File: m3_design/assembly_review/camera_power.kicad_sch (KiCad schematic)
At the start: 22 parts, among them U7 TPS259570DSGR, U8 AP63200WU-7

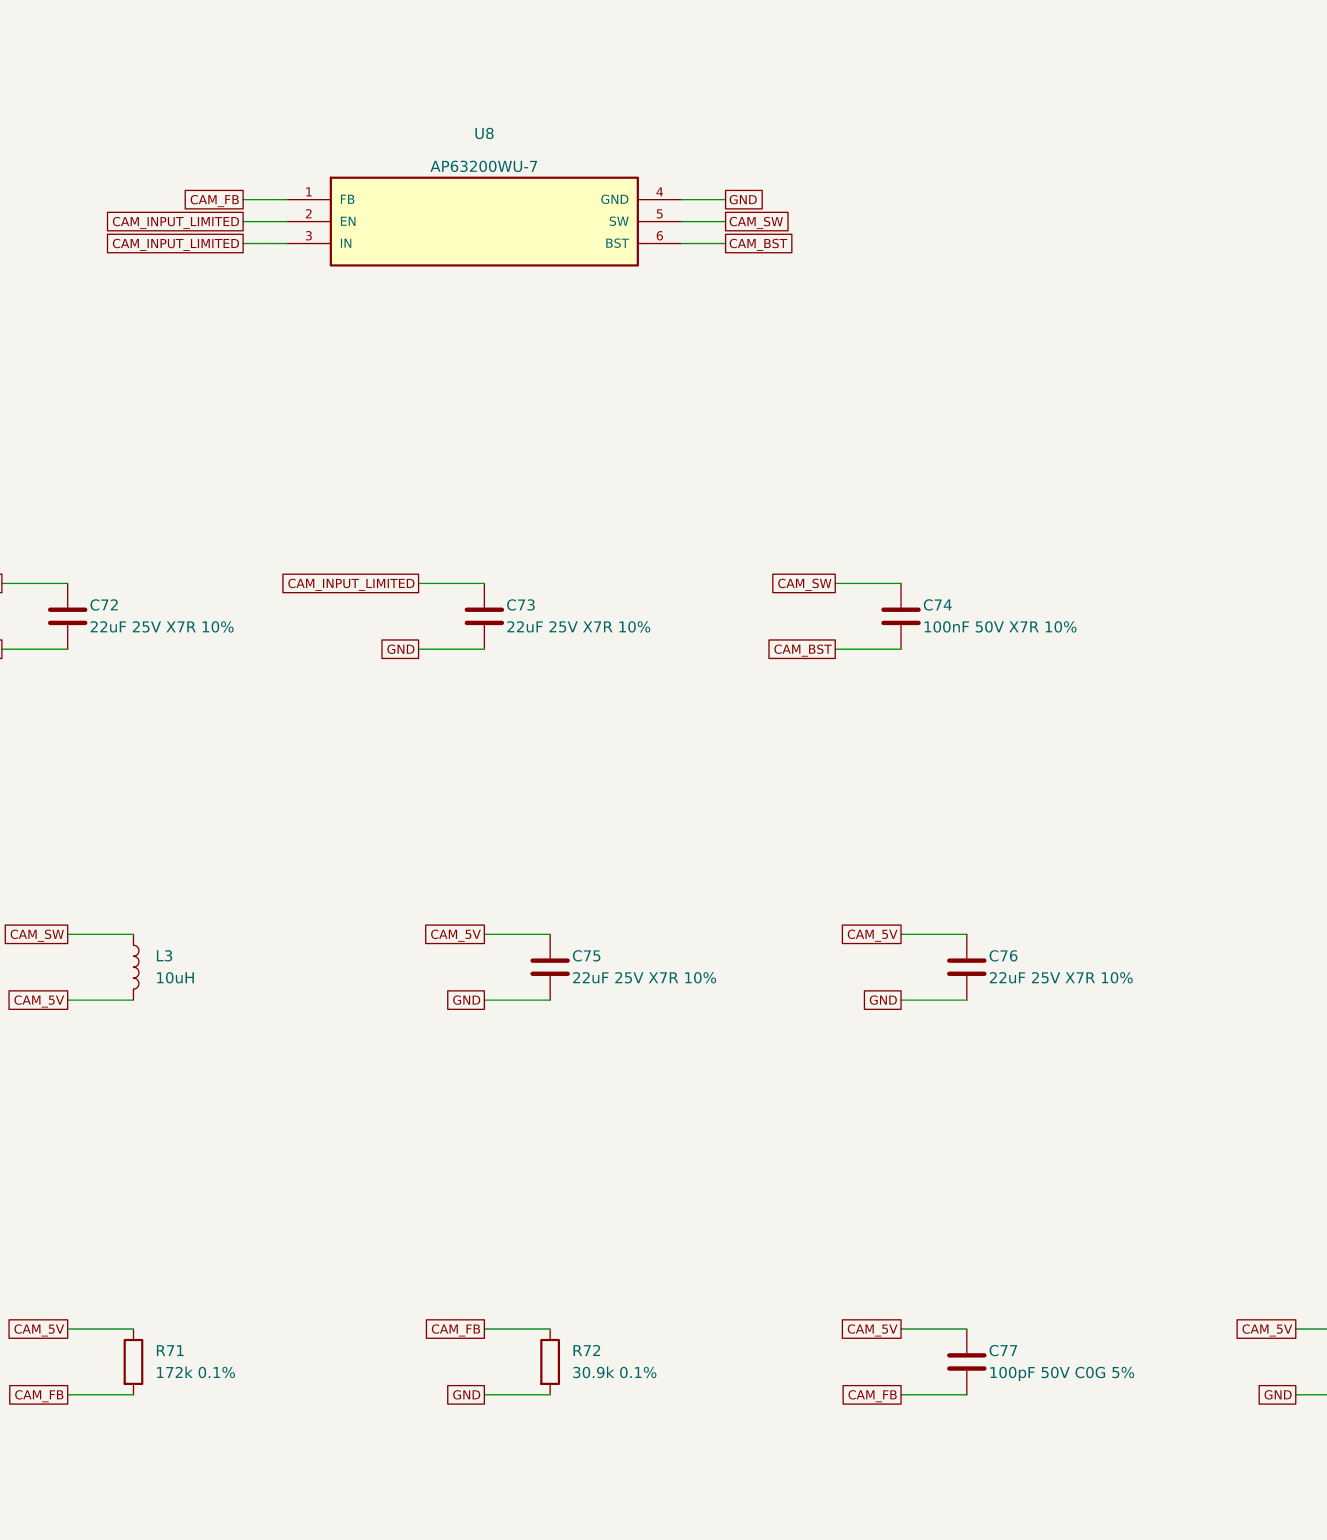
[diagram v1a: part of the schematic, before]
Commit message: Make R2 orderable: stocked drop-ins, JLC placement corrections, ordering guide
- Stock (JLC assembly API): U8 AP63200 -> AP63300WU-7 (same TSOT26 pinout,
  VFB, fsw), L3 -> SRP5030T-6R8M (same body/land, AP63300 Table 1), C77
  100p -> 47p (Table 1), C84 25SVPF330M -> 35SVPK330M (same OS-CON F12).
  Every BOM line now has JLC stock for 5 boards except U6 SAM-M10Q
  (consign / Global Sourcing; DigiKey has stock).
- tools/jlc_orient.py matches each footprint pad-by-pad to the LCSC/EasyEDA
  footprint of its LCSC code; export_fab.py applies the rotation/offset.
  Without it U7, U8, U10, U11, U12, U13, D121 and LED2 would be rotated.
- tools/jlc_stock.py: repeatable stock check; fab/stock_check.json.
- JLC_Assembly field: U6 consign note, J2/J123 hand-cut from one 1x40 strip.
- docs/ORDERING.md: PCB options, PCBA, preview checklist, off-board parts.

DRC 0 / unconnected 0 / parity 0 / ERC 0, audit OK; contract OK;
tests 173/112/12 pass; sim 135 PASS.

Co-Authored-By: Claude Opus 5.5 (1M context) <noreply@anthropic.com>
Claude-Session: https://claude.ai/code/session_01DdkfTxR7SVyv9xZNmPk9vB
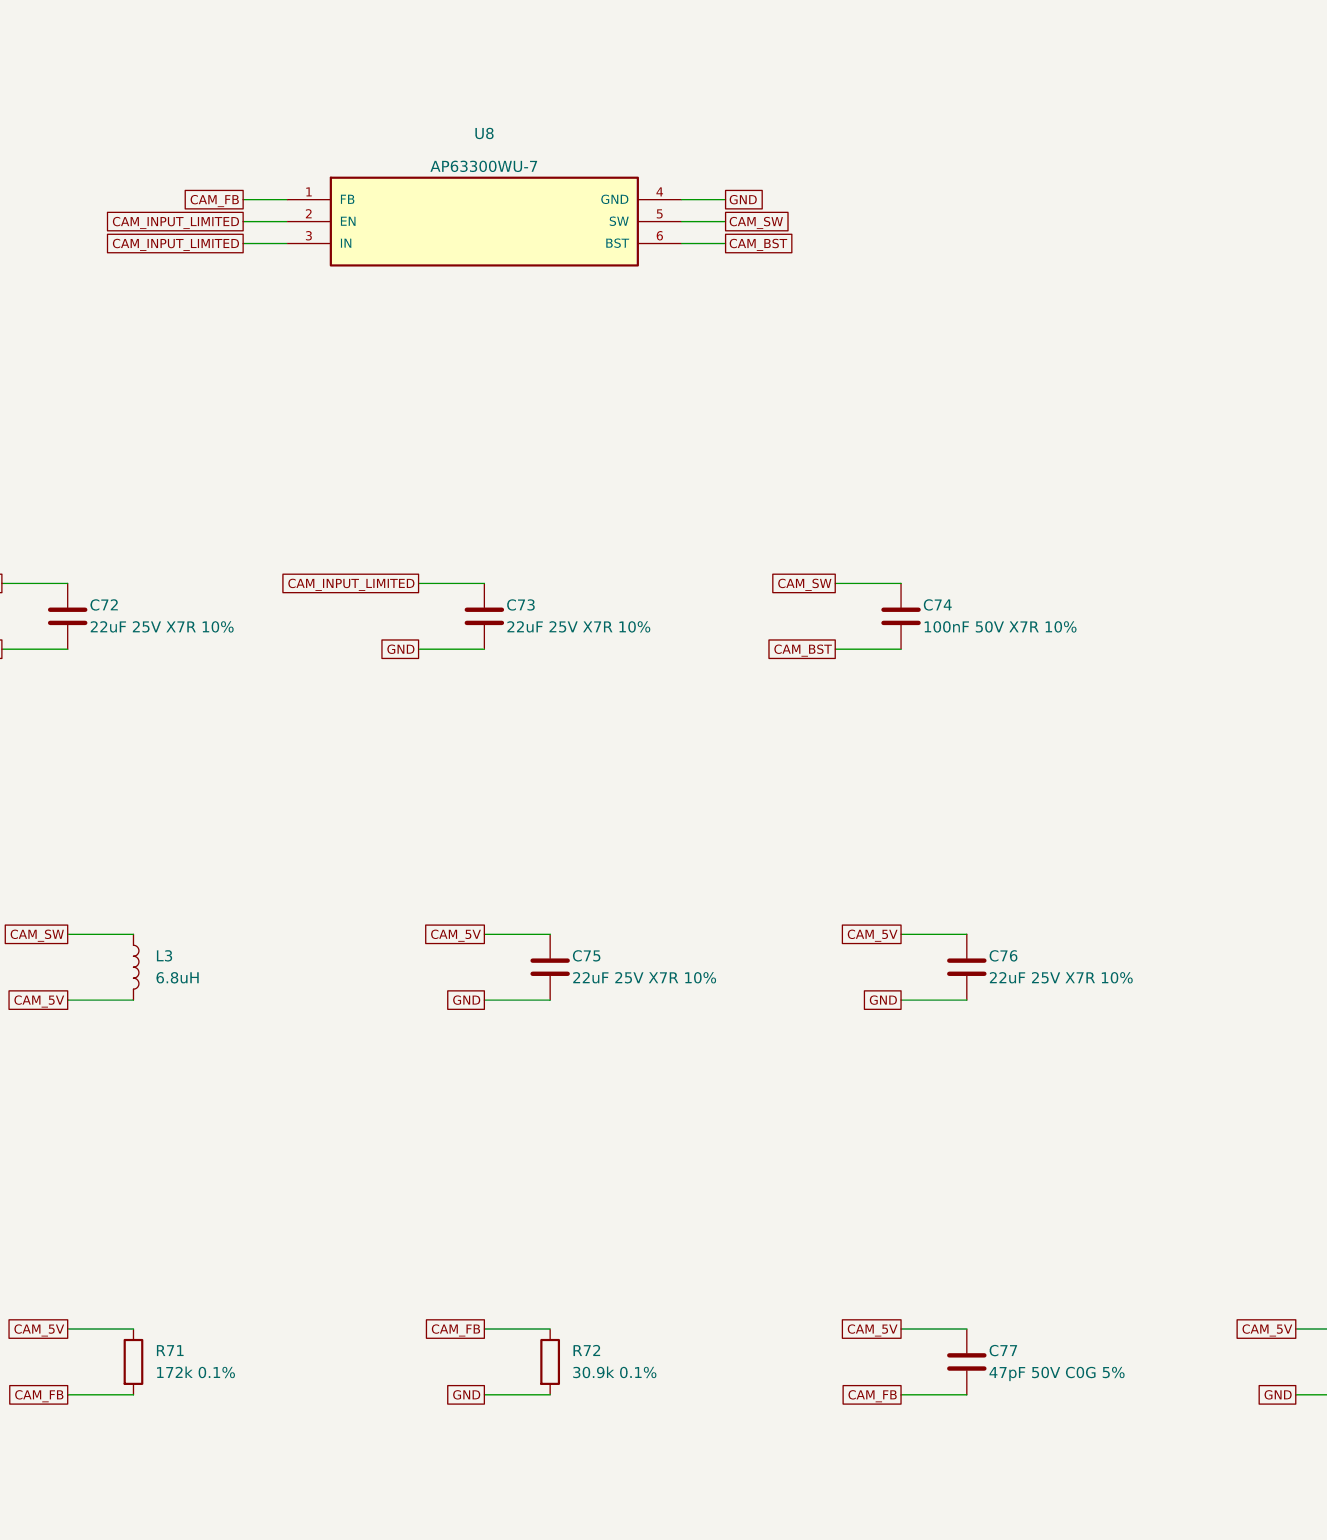
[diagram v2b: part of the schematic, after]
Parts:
- C77: value 100pF 50V C0G 5% -> 47pF 50V C0G 5%; LCSC C14858 -> C1671; LCSC Part C14858 -> C1671; Manufacturer Part CL10C101JB8NNNC -> CL10C470JB8NNNC
- L3: value 10uH -> 6.8uH; LCSC C3223923 -> C1329837; LCSC Part C3223923 -> C1329837; Manufacturer Part SRP5030TA-100M -> SRP5030T-6R8M
- U8: value AP63200WU-7 -> AP63300WU-7; LCSC C2071868 -> C2158012
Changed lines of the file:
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@@
 				(font
 					(size 1.27 1.27))))
-		(property "Value" "AP63200WU-7"
+		(property "Value" "AP63300WU-7"
 			(at 276.86 69.85 0)
 			(effects
@@
 				(font
 					(size 1.27 1.27))))
-		(property "LCSC" "C2071868"
+		(property "LCSC" "C2158012"
 			(at 276.86 76.2 0)
 			(hide yes)
@@
 					(size 1.27 1.27))
 				(justify left)))
-		(property "Value" "10uH"
+		(property "Value" "6.8uH"
 			(at 238.76 163.82999999999998 0)
 			(effects
@@
 					(size 1.27 1.27))
 				(justify left)))
-		(property "LCSC" "C3223923"
+		(property "LCSC" "C1329837"
 			(at 236.22 162.56 0)
 			(hide yes)
@@
 				(font
 					(size 1.27 1.27))))
-		(property "Manufacturer Part" "SRP5030TA-100M"
+		(property "Manufacturer Part" "SRP5030T-6R8M"
 			(at 236.22 162.56 0)
 			(hide yes)
@@
 				(font
 					(size 1.27 1.27))))
-		(property "LCSC Part" "C3223923"
+		(property "LCSC Part" "C1329837"
 			(at 236.22 162.56 0)
 			(hide yes)
@@
 					(size 1.27 1.27))
 				(justify left)))
-		(property "Value" "100pF 50V C0G 5%"
+		(property "Value" "47pF 50V C0G 5%"
 			(at 335.28000000000003 209.54999999999998 0)
 			(effects
@@
 					(size 1.27 1.27))
 				(justify left)))
-		(property "LCSC" "C14858"
+		(property "LCSC" "C1671"
 			(at 332.74 208.28 0)
 			(hide yes)
@@
 				(font
 					(size 1.27 1.27))))
-		(property "Manufacturer Part" "CL10C101JB8NNNC"
+		(property "Manufacturer Part" "CL10C470JB8NNNC"
 			(at 332.74 208.28 0)
 			(hide yes)
@@
 				(font
 					(size 1.27 1.27))))
-		(property "LCSC Part" "C14858"
+		(property "LCSC Part" "C1671"
 			(at 332.74 208.28 0)
 			(hide yes)

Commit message: M3-ASSY-R3: 1k 1% resistors to JLC Basic, regenerate fab package, cost gate
R74/R77/R100/R101/R103: C22548 (Yageo RC0603FR-071KL) -> C21190 (UNI-ROYAL
0603WAF1001T5E), same 1k 1% 100 ppm 0.1 W 75 V 0603 land. The 100 nF C1591 ->
C14663 swap was not made: C128/C140 sit on the pyro outputs and no DC-bias data
exists for the replacement, so the line stays extended either way.
jlc_orient: C21190 via a same-footprint donor (EasyEDA API returned 403).
export_fab: 75 lines, 180 placed, no missing LCSC, no unverified rotation.
jlc_stock --boards 5: short only U4 ICM-45686 (JLC stock 0, protected).
jlc_cost: parts $54.94/board at 5 boards, 48 unique extended codes (gate counts
codes, not rows). check.sh all zero.

Co-Authored-By: Claude Opus 5.5 <noreply@anthropic.com>
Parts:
- R74, R77: LCSC C22548 -> C21190; LCSC Part C22548 -> C21190; Manufacturer Yageo -> UNI-ROYAL(Uniroyal Elec); Manufacturer Part RC0603FR-071KL -> 0603WAF1001T5E
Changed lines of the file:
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@@
 					(size 1.27 1.27))
 				(justify left)))
-		(property "LCSC" "C22548"
+		(property "LCSC" "C21190"
 			(at 53.34 213.36 0)
 			(hide yes)
@@
 					(reference "R74")
 					(unit 1))))
-		(property "Manufacturer" "Yageo"
+		(property "Manufacturer" "UNI-ROYAL(Uniroyal Elec)"
 			(at 53.34 213.36 0)
 			(hide yes)
@@
 				(font
 					(size 1.27 1.27))))
-		(property "Manufacturer Part" "RC0603FR-071KL"
+		(property "Manufacturer Part" "0603WAF1001T5E"
 			(at 53.34 213.36 0)
 			(hide yes)
@@
 				(font
 					(size 1.27 1.27))))
-		(property "LCSC Part" "C22548"
+		(property "LCSC Part" "C21190"
 			(at 53.34 213.36 0)
 			(hide yes)
@@
 					(size 1.27 1.27))
 				(justify left)))
-		(property "LCSC" "C22548"
+		(property "LCSC" "C21190"
 			(at 104.14 254 0)
 			(hide yes)
@@
 					(reference "R77")
 					(unit 1))))
-		(property "Manufacturer" "Yageo"
-			(at 104.14 254 0)
-			(hide yes)
-			(effects
-				(font
-					(size 1.27 1.27))))
-		(property "Manufacturer Part" "RC0603FR-071KL"
-			(at 104.14 254 0)
-			(hide yes)
-			(effects
-				(font
-					(size 1.27 1.27))))
-		(property "LCSC Part" "C22548"
-			(at 104.14 254 0)
-			(hide yes)
+		(property "Manufacturer" "UNI-ROYAL(Uniroyal Elec)"
+			(at 104.14 254 0)
+			(hide yes)
+			(effects
+				(font
+					(size 1.27 1.27))))
+		(property "Manufacturer Part" "0603WAF1001T5E"
+			(at 104.14 254 0)
+			(hide yes)
+			(effects
+				(font
+					(size 1.27 1.27))))
+		(property "LCSC Part" "C21190"
+			(at 104.14 254 0)
+			(hide yes)
